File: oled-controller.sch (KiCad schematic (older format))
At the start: 3 parts

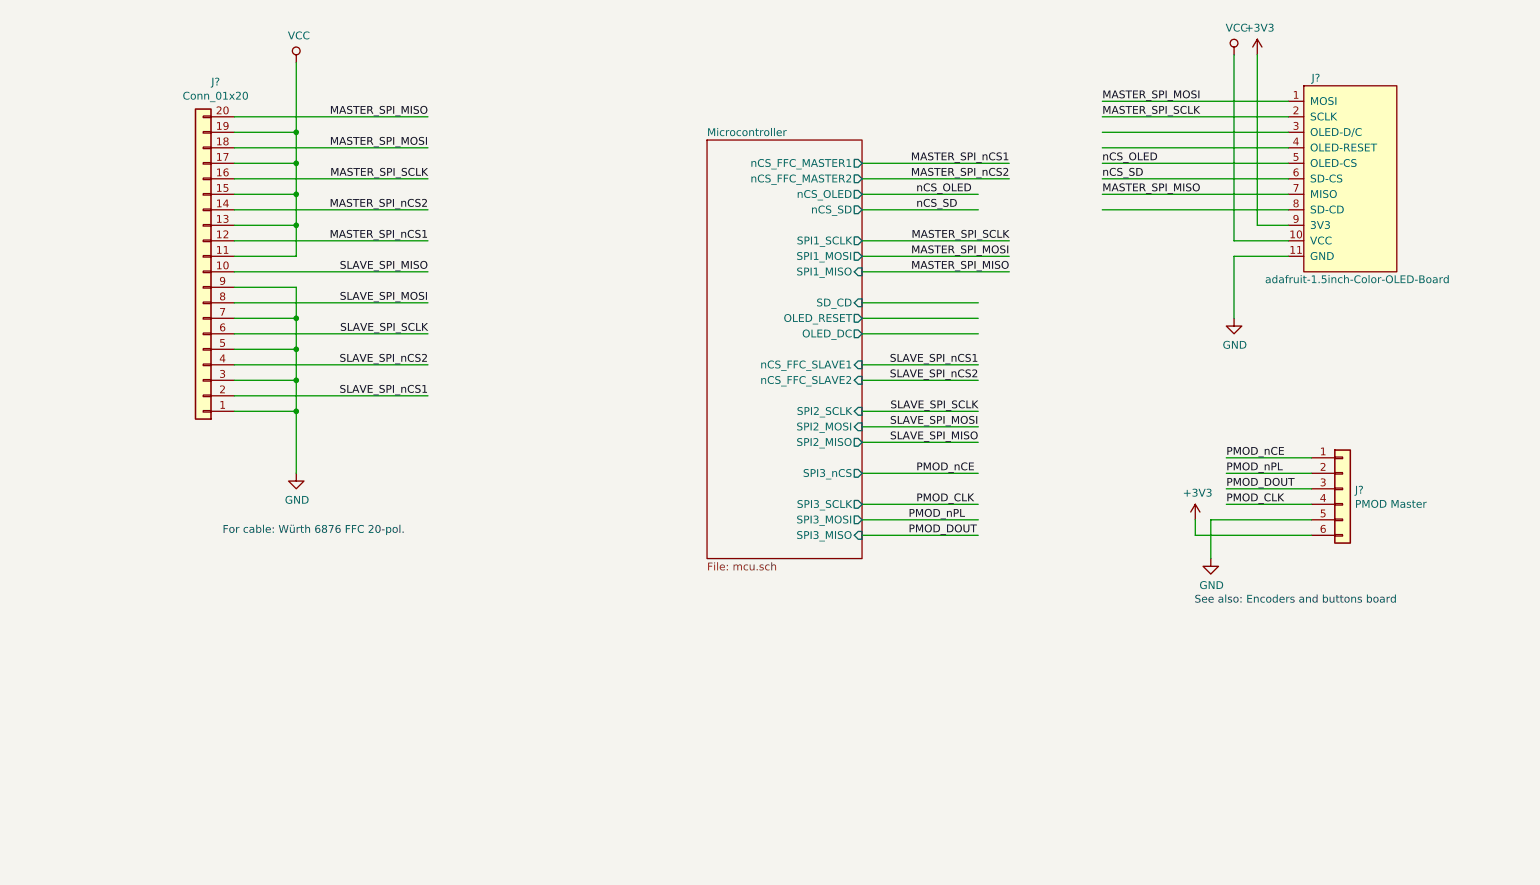
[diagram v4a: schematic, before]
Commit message: Completed schematic adjustments and layouting
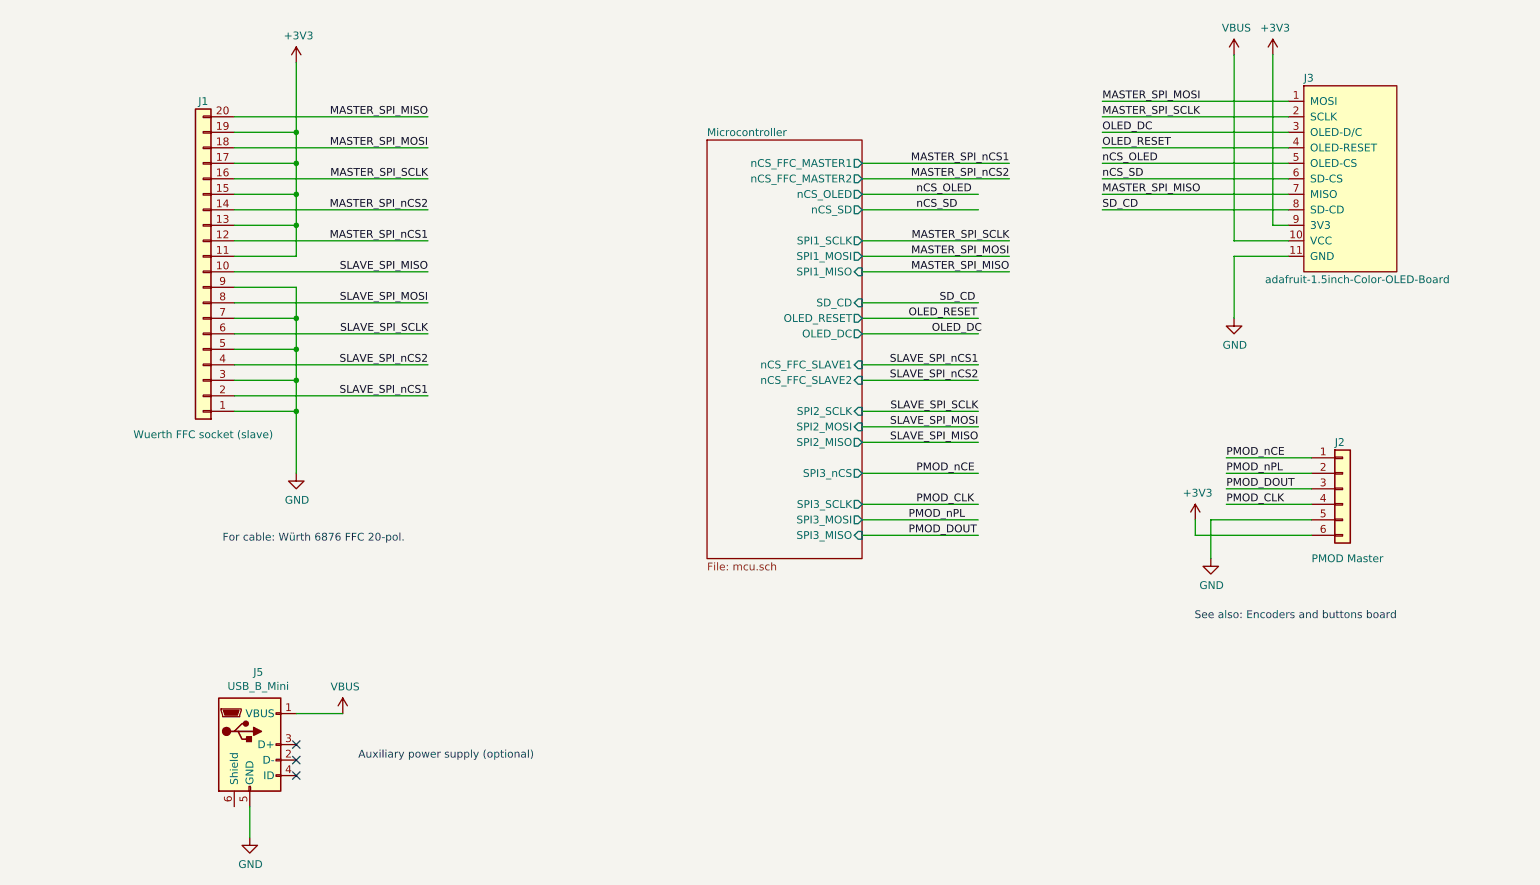
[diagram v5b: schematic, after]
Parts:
- added J5: USB_B_Mini, Connector_USB:USB_Mini-B_Lumberg_2486_01_Horizontal, symbol Connector:USB_B_Mini
- J1: renamed from J?; value Conn_01x20 -> Wuerth FFC socket (slave); footprint (none) -> Matthias:Wuerth_687120149022_1x20-1MP_P0.5mm_Horizontal_Handsolder
- J3: renamed from J?; footprint Connector_PinSocket_2.54mm:PinSocket_1x11_P2.54mm_Vertical -> Matthias:Adafruit-1.5inch-Color-OLED-PCB
- gave numbers to parts that had none: 1
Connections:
- net labels added: OLED_DC, OLED_RESET, SD_CD, VBUS
- net labels removed: VCC
- wire segments 71 -> 73
- no-connect marks 0 -> 3
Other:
- note added: "Auxiliary power supply (optional)"
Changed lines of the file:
@@
 $EndDescr
 $Comp
-L Matthias:adafruit-1.5inch-Color-OLED-Board J?
+L Matthias:adafruit-1.5inch-Color-OLED-Board J3
 U 1 1 5C79A0AF
 P 9400 2550
-F 0 "J?" H 9150 3200 50  0000 L CNN
+F 0 "J3" H 9100 3200 50  0000 L CNN
 F 1 "adafruit-1.5inch-Color-OLED-Board" H 8850 1900 50  0000 L CNN
-F 2 "Connector_PinSocket_2.54mm:PinSocket_1x11_P2.54mm_Vertical" H 9200 2600 50  0001 C CNN
+F 2 "Matthias:Adafruit-1.5inch-Color-OLED-PCB" H 9200 2600 50  0001 C CNN
 F 3 "" H 9200 2600 50  0001 C CNN
 	1    9400 2550
@@
 $EndComp
 $Comp
-L Connector_Generic:Conn_01x20 J?
+L Connector_Generic:Conn_01x20 J1
 U 1 1 5CA0EBAD
 P 2000 3150
-F 0 "J?" H 1920 1925 50  0000 C CNN
-F 1 "Conn_01x20" H 1920 2016 50  0000 C CNN
-F 2 "" H 2000 3150 50  0001 C CNN
+F 0 "J1" H 2000 2050 50  0000 C CNN
+F 1 "Wuerth FFC socket (slave)" H 2000 4200 50  0000 C CNN
+F 2 "Matthias:Wuerth_687120149022_1x20-1MP_P0.5mm_Horizontal_Handsolder" H 2000 3150 50  0001 C CNN
 F 3 "~" H 2000 3150 50  0001 C CNN
 	1    2000 3150
@@
 	2600 2250 2600 1800
 $Comp
-L power:+3V3 #PWR?
+L power:+3V3 #PWR0101
 U 1 1 5CA0F539
-P 8800 1750
-F 0 "#PWR?" H 8800 1600 50  0001 C CNN
-F 1 "+3V3" H 8815 1923 50  0000 C CNN
-F 2 "" H 8800 1750 50  0001 C CNN
-F 3 "" H 8800 1750 50  0001 C CNN
-	1    8800 1750
-	1    0    0    -1
-$EndComp
-$Comp
-L power:GND #PWR?
+P 8900 1750
+F 0 "#PWR0101" H 8900 1600 50  0001 C CNN
+F 1 "+3V3" H 8915 1923 50  0000 C CNN
+F 2 "" H 8900 1750 50  0001 C CNN
+F 3 "" H 8900 1750 50  0001 C CNN
+	1    8900 1750
+	1    0    0    -1
+$EndComp
+$Comp
+L power:GND #PWR0102
 U 1 1 5CA0F568
 P 2600 4450
-F 0 "#PWR?" H 2600 4200 50  0001 C CNN
+F 0 "#PWR0102" H 2600 4200 50  0001 C CNN
 F 1 "GND" H 2605 4277 50  0000 C CNN
 F 2 "" H 2600 4450 50  0001 C CNN
@@
 	1    0    0    -1
 $EndComp
-Text Notes 3300 4850 2    50   ~ 0
+Text Notes 3300 4900 2    50   ~ 0
 For cable: Würth 6876 FFC 20-pol.
 Wire Wire Line
@@
 	9000 2750 7800 2750
 Wire Wire Line
-	9000 2850 8800 2850
-Wire Wire Line
-	8800 2850 8800 1750
-$Comp
-L power:VCC #PWR?
-U 1 1 5CA16F17
-P 2600 1800
-F 0 "#PWR?" H 2600 1650 50  0001 C CNN
-F 1 "VCC" H 2617 1973 50  0000 C CNN
-F 2 "" H 2600 1800 50  0001 C CNN
-F 3 "" H 2600 1800 50  0001 C CNN
-	1    2600 1800
-	1    0    0    -1
-$EndComp
+	9000 2850 8900 2850
+Wire Wire Line
+	8900 2850 8900 1750
 Wire Wire Line
 	9000 2950 8650 2950
 Wire Wire Line
 	8650 2950 8650 1750
-$Comp
-L power:VCC #PWR?
-U 1 1 5CA186FF
-P 8650 1750
-F 0 "#PWR?" H 8650 1600 50  0001 C CNN
-F 1 "VCC" H 8667 1923 50  0000 C CNN
-F 2 "" H 8650 1750 50  0001 C CNN
-F 3 "" H 8650 1750 50  0001 C CNN
-	1    8650 1750
-	1    0    0    -1
-$EndComp
 Wire Wire Line
 	9000 3050 8650 3050
@@
 	8650 3050 8650 3450
 $Comp
-L power:GND #PWR?
+L power:GND #PWR0105
 U 1 1 5CA190CF
 P 8650 3450
-F 0 "#PWR?" H 8650 3200 50  0001 C CNN
+F 0 "#PWR0105" H 8650 3200 50  0001 C CNN
 F 1 "GND" H 8655 3277 50  0000 C CNN
 F 2 "" H 8650 3450 50  0001 C CNN
@@
 	6250 4850 7000 4850
 $Comp
-L Connector_Generic:Conn_01x06 J?
+L Connector_Generic:Conn_01x06 J2
 U 1 1 5CA45764
 P 9350 4550
-F 0 "J?" H 9430 4542 50  0000 L CNN
-F 1 "PMOD Master" H 9430 4451 50  0000 L CNN
+F 0 "J2" H 9300 4850 50  0000 L CNN
+F 1 "PMOD Master" H 9150 4100 50  0000 L CNN
 F 2 "Connector_PinHeader_2.54mm:PinHeader_1x06_P2.54mm_Vertical" H 9350 4550 50  0001 C CNN
 F 3 "~" H 9350 4550 50  0001 C CNN
@@
 Wire Wire Line
 	9150 4750 8500 4750
-Text Notes 9700 5300 2    50   ~ 0
+Text Notes 9700 5400 2    50   ~ 0
 See also: Encoders and buttons board
 Text Label 8600 4350 0    50   ~ 0
@@
 	8500 4750 8500 5000
 $Comp
-L power:GND #PWR?
+L power:GND #PWR0106
 U 1 1 5CA56BF4
 P 8500 5000
-F 0 "#PWR?" H 8500 4750 50  0001 C CNN
+F 0 "#PWR0106" H 8500 4750 50  0001 C CNN
 F 1 "GND" H 8505 4827 50  0000 C CNN
 F 2 "" H 8500 5000 50  0001 C CNN
@@
 	8400 4850 9150 4850
 $Comp
-L power:+3V3 #PWR?
+L power:+3V3 #PWR0107
 U 1 1 5CA59B37
 P 8400 4750
-F 0 "#PWR?" H 8400 4600 50  0001 C CNN
+F 0 "#PWR0107" H 8400 4600 50  0001 C CNN
 F 1 "+3V3" H 8415 4923 50  0000 C CNN
 F 2 "" H 8400 4750 50  0001 C CNN
@@
 Text Label 7000 4250 2    50   ~ 0
 SLAVE_SPI_MISO
+Text Label 7800 2750 0    50   ~ 0
+SD_CD
+Text Label 6750 3350 0    50   ~ 0
+SD_CD
+Text Label 7800 2250 0    50   ~ 0
+OLED_DC
+Text Label 6700 3550 0    50   ~ 0
+OLED_DC
+Text Label 7800 2350 0    50   ~ 0
+OLED_RESET
+Text Label 6550 3450 0    50   ~ 0
+OLED_RESET
+$Comp
+L Connector:USB_B_Mini J5
+U 1 1 5CA4C155
+P 2300 6200
+F 0 "J5" H 2355 6667 50  0000 C CNN
+F 1 "USB_B_Mini" H 2355 6576 50  0000 C CNN
+F 2 "Connector_USB:USB_Mini-B_Lumberg_2486_01_Horizontal" H 2450 6150 50  0001 C CNN
+F 3 "~" H 2450 6150 50  0001 C CNN
+	1    2300 6200
+	1    0    0    -1
+$EndComp
+$Comp
+L power:+3V3 #PWR0103
+U 1 1 5CA4C221
+P 2600 1800
+F 0 "#PWR0103" H 2600 1650 50  0001 C CNN
+F 1 "+3V3" H 2615 1973 50  0000 C CNN
+F 2 "" H 2600 1800 50  0001 C CNN
+F 3 "" H 2600 1800 50  0001 C CNN
+	1    2600 1800
+	1    0    0    -1
+$EndComp
+$Comp
+L power:VBUS #PWR0104
+U 1 1 5CA4C3FC
+P 8650 1750
+F 0 "#PWR0104" H 8650 1600 50  0001 C CNN
+F 1 "VBUS" H 8665 1923 50  0000 C CNN
+F 2 "" H 8650 1750 50  0001 C CNN
+F 3 "" H 8650 1750 50  0001 C CNN
+	1    8650 1750
+	1    0    0    -1
+$EndComp
+$Comp
+L power:VBUS #PWR0122
+U 1 1 5CA51035
+P 2900 6000
+F 0 "#PWR0122" H 2900 5850 50  0001 C CNN
+F 1 "VBUS" H 2915 6173 50  0000 C CNN
+F 2 "" H 2900 6000 50  0001 C CNN
+F 3 "" H 2900 6000 50  0001 C CNN
+	1    2900 6000
+	1    0    0    -1
+$EndComp
+$Comp
+L power:GND #PWR0123
+U 1 1 5CA5112B
+P 2300 6800
+F 0 "#PWR0123" H 2300 6550 50  0001 C CNN
+F 1 "GND" H 2305 6627 50  0000 C CNN
+F 2 "" H 2300 6800 50  0001 C CNN
+F 3 "" H 2300 6800 50  0001 C CNN
+	1    2300 6800
+	1    0    0    -1
+$EndComp
+NoConn ~ 2600 6200
+NoConn ~ 2600 6300
+NoConn ~ 2600 6400
+Wire Wire Line
+	2900 6000 2600 6000
+Wire Wire Line
+	2300 6600 2300 6800
+Text Notes 3000 6300 0    50   ~ 0
+Auxiliary power supply (optional)
 $EndSCHEMATC

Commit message: Added two LEDs
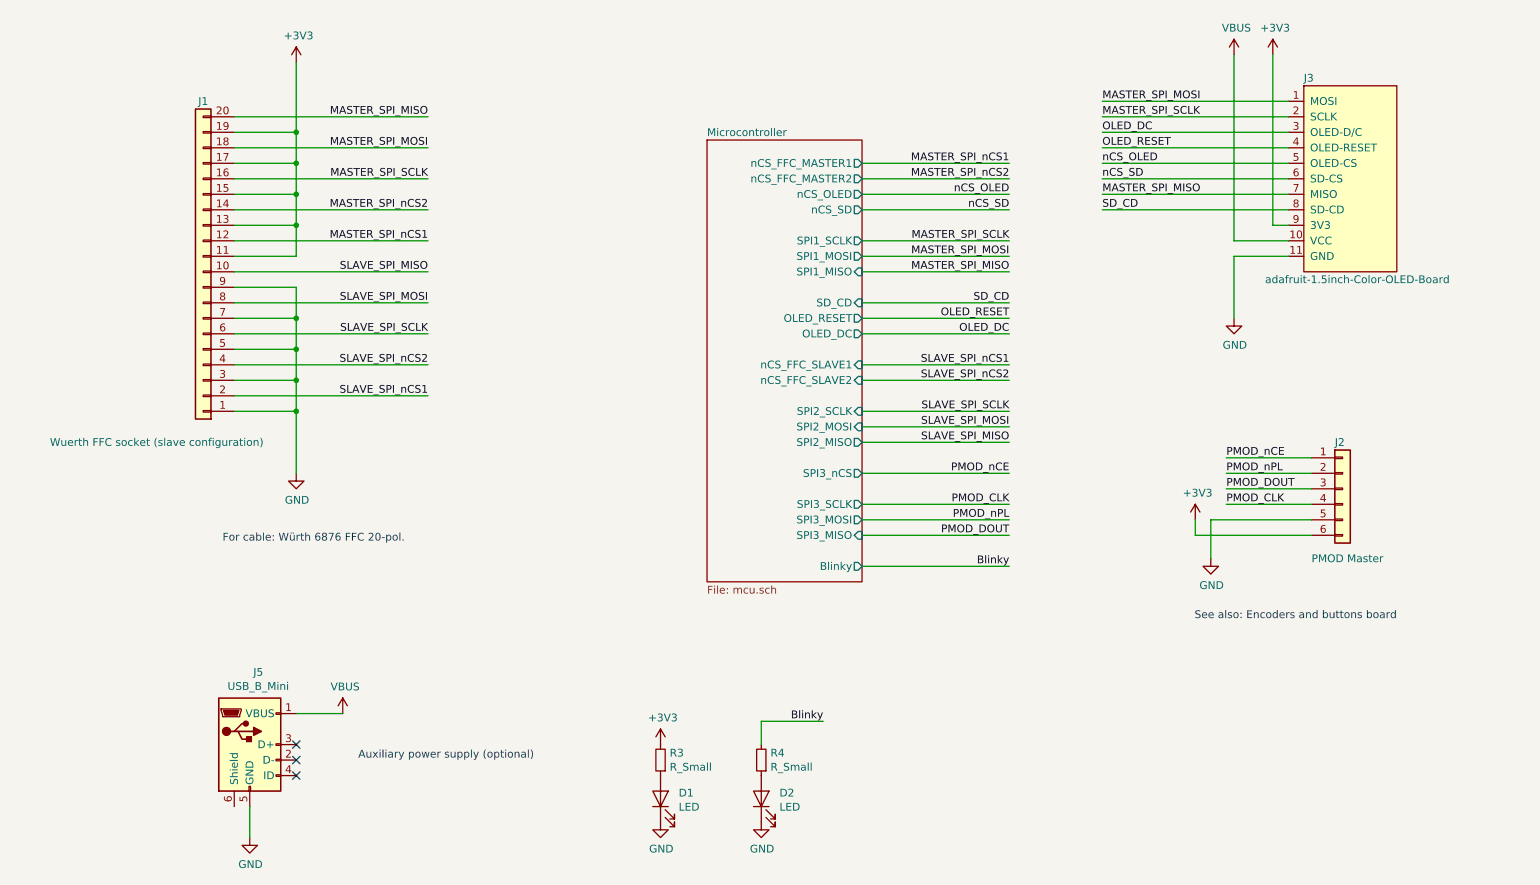
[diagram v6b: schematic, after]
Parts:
- added D1, D2: LED, Diode_SMD:D_0603_1608Metric_Pad1.05x0.95mm_HandSolder, symbol Device:LED
- added R3, R4: R_Small, Resistor_SMD:R_0603_1608Metric_Pad1.05x0.95mm_HandSolder, symbol Device:R_Small
- J1: value Wuerth FFC socket (slave) -> Wuerth FFC socket (slave configuration)
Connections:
- net labels added: Blinky
- wire segments 73 -> 76
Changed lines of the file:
@@
 P 2000 3150
 F 0 "J1" H 2000 2050 50  0000 C CNN
-F 1 "Wuerth FFC socket (slave)" H 2000 4200 50  0000 C CNN
+F 1 "Wuerth FFC socket (slave configuration)" H 2300 4250 50  0000 C CNN
 F 2 "Matthias:Wuerth_687120149022_1x20-1MP_P0.5mm_Horizontal_Handsolder" H 2000 3150 50  0001 C CNN
 F 3 "~" H 2000 3150 50  0001 C CNN
@@
 	6250 2550 7200 2550
 Wire Wire Line
-	6250 2650 7000 2650
-Wire Wire Line
-	6250 2750 7000 2750
+	6250 2650 7200 2650
+Wire Wire Line
+	6250 2750 7200 2750
 Wire Wire Line
 	6250 2950 7200 2950
@@
 	6250 3150 7200 3150
 Wire Wire Line
-	6250 3350 7000 3350
-Wire Wire Line
-	6250 3450 7000 3450
-Wire Wire Line
-	6250 3750 7000 3750
-Wire Wire Line
-	6250 3850 7000 3850
-Wire Wire Line
-	6250 4050 7000 4050
-Wire Wire Line
-	6250 4150 7000 4150
-Wire Wire Line
-	6250 4250 7000 4250
-Wire Wire Line
-	6250 4450 7000 4450
-Wire Wire Line
-	6250 4650 7000 4650
-Wire Wire Line
-	6250 4750 7000 4750
-Wire Wire Line
-	6250 4850 7000 4850
+	6250 3350 7200 3350
+Wire Wire Line
+	6250 3450 7200 3450
+Wire Wire Line
+	6250 3750 7200 3750
+Wire Wire Line
+	6250 3850 7200 3850
+Wire Wire Line
+	6250 4050 7200 4050
+Wire Wire Line
+	6250 4150 7200 4150
+Wire Wire Line
+	6250 4250 7200 4250
+Wire Wire Line
+	6250 4450 7200 4450
+Wire Wire Line
+	6250 4650 7200 4650
+Wire Wire Line
+	6250 4750 7200 4750
+Wire Wire Line
+	6250 4850 7200 4850
 $Comp
 L Connector_Generic:Conn_01x06 J2
@@
 Text Label 7800 2450 0    50   ~ 0
 nCS_OLED
-Text Label 6600 2650 0    50   ~ 0
+Text Label 7200 2650 2    50   ~ 0
 nCS_OLED
 Text Label 7800 2550 0    50   ~ 0
 nCS_SD
-Text Label 6600 2750 0    50   ~ 0
+Text Label 7200 2750 2    50   ~ 0
 nCS_SD
 Text Label 7200 2950 2    50   ~ 0
@@
 Text Label 7200 3150 2    50   ~ 0
 MASTER_SPI_MISO
-Text Label 6600 4650 0    50   ~ 0
+Text Label 7200 4650 2    50   ~ 0
 PMOD_CLK
-Text Label 6550 4850 0    50   ~ 0
+Text Label 7200 4850 2    50   ~ 0
 PMOD_DOUT
-Text Label 6550 4750 0    50   ~ 0
+Text Label 7200 4750 2    50   ~ 0
 PMOD_nPL
-Text Label 6600 4450 0    50   ~ 0
+Text Label 7200 4450 2    50   ~ 0
 PMOD_nCE
 $Sheet
-S 5250 2300 1000 2700
+S 5250 2300 1000 2850
 U 5C795DEE
 F0 "Microcontroller" 50
@@
 F19 "nCS_FFC_SLAVE2" I R 6250 3850 50
 F20 "OLED_DC" O R 6250 3550 50
+F21 "Blinky" O R 6250 5050 50
 $EndSheet
 Wire Wire Line
-	6250 3550 7000 3550
-Text Label 7000 3750 2    50   ~ 0
+	6250 3550 7200 3550
+Text Label 7200 3750 2    50   ~ 0
 SLAVE_SPI_nCS1
-Text Label 7000 3850 2    50   ~ 0
+Text Label 7200 3850 2    50   ~ 0
 SLAVE_SPI_nCS2
-Text Label 7000 4050 2    50   ~ 0
+Text Label 7200 4050 2    50   ~ 0
 SLAVE_SPI_SCLK
-Text Label 7000 4150 2    50   ~ 0
+Text Label 7200 4150 2    50   ~ 0
 SLAVE_SPI_MOSI
-Text Label 7000 4250 2    50   ~ 0
+Text Label 7200 4250 2    50   ~ 0
 SLAVE_SPI_MISO
 Text Label 7800 2750 0    50   ~ 0
 SD_CD
-Text Label 6750 3350 0    50   ~ 0
+Text Label 7200 3350 2    50   ~ 0
 SD_CD
 Text Label 7800 2250 0    50   ~ 0
 OLED_DC
-Text Label 6700 3550 0    50   ~ 0
+Text Label 7200 3550 2    50   ~ 0
 OLED_DC
 Text Label 7800 2350 0    50   ~ 0
 OLED_RESET
-Text Label 6550 3450 0    50   ~ 0
+Text Label 7200 3450 2    50   ~ 0
 OLED_RESET
 $Comp
@@
 Text Notes 3000 6300 0    50   ~ 0
 Auxiliary power supply (optional)
+$Comp
+L Device:LED D1
+U 1 1 5CA80EEE
+P 4950 6550
+F 0 "D1" V 4988 6433 50  0000 R CNN
+F 1 "LED" V 4897 6433 50  0000 R CNN
+F 2 "Diode_SMD:D_0603_1608Metric_Pad1.05x0.95mm_HandSolder" H 4950 6550 50  0001 C CNN
+F 3 "~" H 4950 6550 50  0001 C CNN
+	1    4950 6550
+	0    -1   -1   0
+$EndComp
+$Comp
+L Device:R_Small R3
+U 1 1 5CA81041
+P 4950 6300
+F 0 "R3" H 4891 6254 50  0000 R CNN
+F 1 "R_Small" H 4891 6345 50  0000 R CNN
+F 2 "Resistor_SMD:R_0603_1608Metric_Pad1.05x0.95mm_HandSolder" H 4950 6300 50  0001 C CNN
+F 3 "~" H 4950 6300 50  0001 C CNN
+	1    4950 6300
+	-1   0    0    1
+$EndComp
+$Comp
+L power:GND #PWR0118
+U 1 1 5CA810C1
+P 4950 6700
+F 0 "#PWR0118" H 4950 6450 50  0001 C CNN
+F 1 "GND" H 4955 6527 50  0000 C CNN
+F 2 "" H 4950 6700 50  0001 C CNN
+F 3 "" H 4950 6700 50  0001 C CNN
+	1    4950 6700
+	1    0    0    -1
+$EndComp
+$Comp
+L power:+3V3 #PWR0119
+U 1 1 5CA81134
+P 4950 6200
+F 0 "#PWR0119" H 4950 6050 50  0001 C CNN
+F 1 "+3V3" H 4965 6373 50  0000 C CNN
+F 2 "" H 4950 6200 50  0001 C CNN
+F 3 "" H 4950 6200 50  0001 C CNN
+	1    4950 6200
+	1    0    0    -1
+$EndComp
+$Comp
+L Device:LED D2
+U 1 1 5CA8323E
+P 5600 6550
+F 0 "D2" V 5638 6433 50  0000 R CNN
+F 1 "LED" V 5547 6433 50  0000 R CNN
+F 2 "Diode_SMD:D_0603_1608Metric_Pad1.05x0.95mm_HandSolder" H 5600 6550 50  0001 C CNN
+F 3 "~" H 5600 6550 50  0001 C CNN
+	1    5600 6550
+	0    -1   -1   0
+$EndComp
+$Comp
+L Device:R_Small R4
+U 1 1 5CA83245
+P 5600 6300
+F 0 "R4" H 5541 6254 50  0000 R CNN
+F 1 "R_Small" H 5541 6345 50  0000 R CNN
+F 2 "Resistor_SMD:R_0603_1608Metric_Pad1.05x0.95mm_HandSolder" H 5600 6300 50  0001 C CNN
+F 3 "~" H 5600 6300 50  0001 C CNN
+	1    5600 6300
+	-1   0    0    1
+$EndComp
+$Comp
+L power:GND #PWR0126
+U 1 1 5CA8324C
+P 5600 6700
+F 0 "#PWR0126" H 5600 6450 50  0001 C CNN
+F 1 "GND" H 5605 6527 50  0000 C CNN
+F 2 "" H 5600 6700 50  0001 C CNN
+F 3 "" H 5600 6700 50  0001 C CNN
+	1    5600 6700
+	1    0    0    -1
+$EndComp
+Wire Wire Line
+	5600 6200 5600 6050
+Wire Wire Line
+	5600 6050 6000 6050
+Text Label 6000 6050 2    50   ~ 0
+Blinky
+Wire Wire Line
+	6250 5050 7200 5050
+Text Label 7200 5050 2    50   ~ 0
+Blinky
 $EndSCHEMATC
